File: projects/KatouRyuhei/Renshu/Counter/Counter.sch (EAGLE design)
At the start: 63 parts

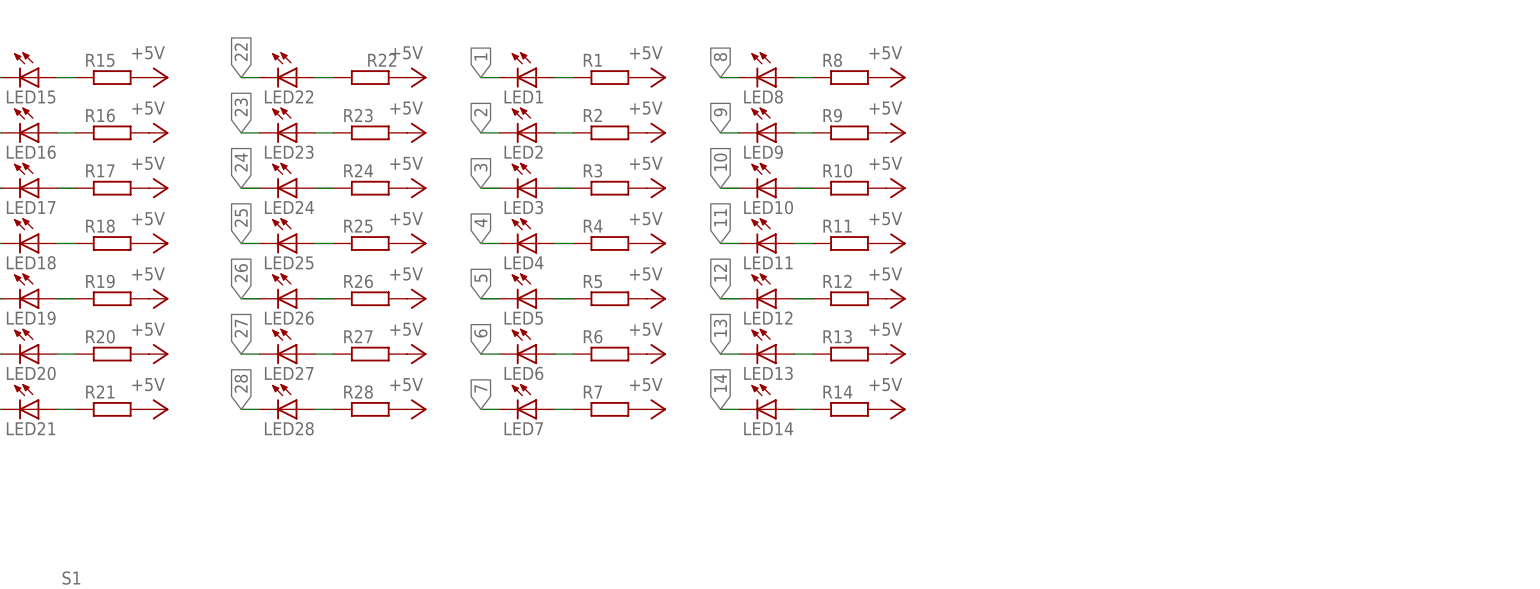
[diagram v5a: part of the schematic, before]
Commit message: 10進数2桁カウンタ製作途中
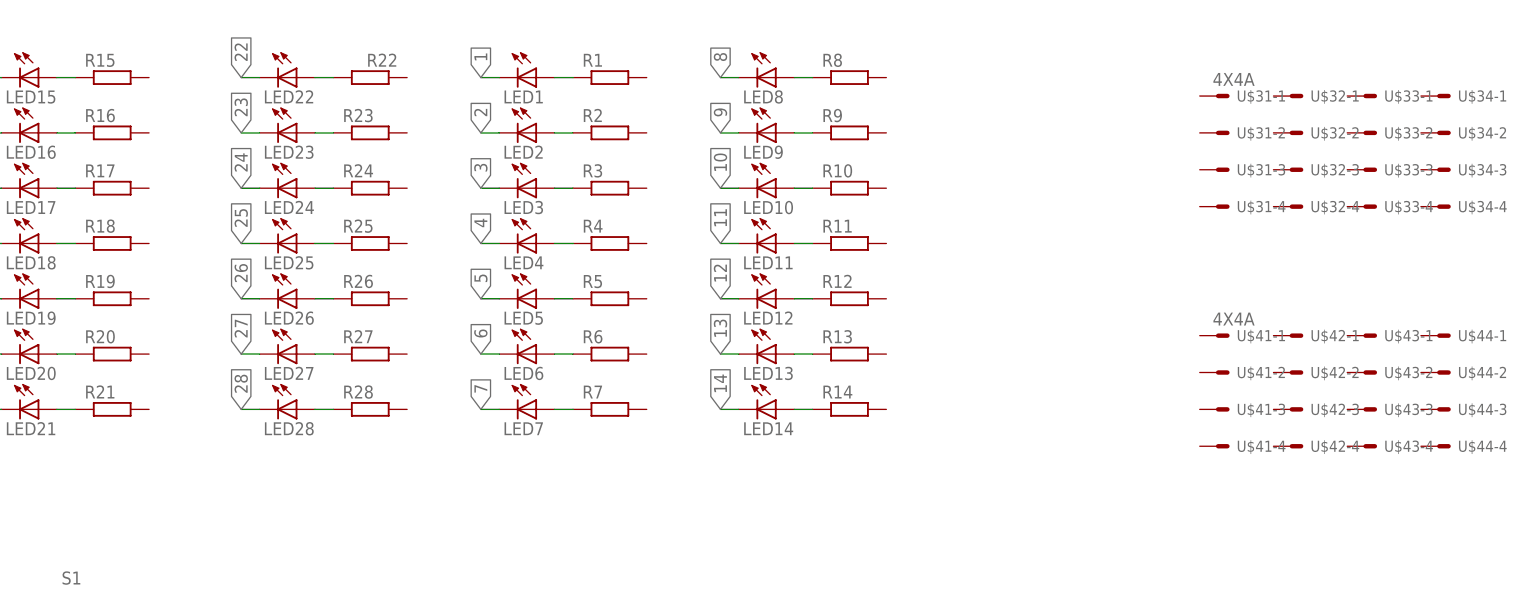
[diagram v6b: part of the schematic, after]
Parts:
- added U$3, U$4: 4X4A, 3M_372xx:4X4A
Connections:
- removed net +5V: R1.2, R10.2, R11.2, R12.2, R13.2, R14.2, R15.2, R16.2, R17.2, R18.2, R19.2, R2.2, R20.2, R21.2, R22.1, R23.2, R24.2, R25.2, R26.2, R27.2, R28.2, R3.2, R4.2, R5.2, R6.2, R7.2, R8.2, R9.2
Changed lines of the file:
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@@
 <part name="GND3" library="supply1" deviceset="GND" device=""/>
 <part name="GND4" library="supply1" deviceset="GND" device=""/>
-<part name="P+1" library="supply1" deviceset="+5V" device=""/>
-<part name="P+2" library="supply1" deviceset="+5V" device=""/>
-<part name="P+3" library="supply1" deviceset="+5V" device=""/>
-<part name="P+4" library="supply1" deviceset="+5V" device=""/>
-<part name="P+5" library="supply1" deviceset="+5V" device=""/>
-<part name="P+6" library="supply1" deviceset="+5V" device=""/>
-<part name="P+7" library="supply1" deviceset="+5V" device=""/>
-<part name="P+8" library="supply1" deviceset="+5V" device=""/>
-<part name="P+9" library="supply1" deviceset="+5V" device=""/>
-<part name="P+10" library="supply1" deviceset="+5V" device=""/>
-<part name="P+11" library="supply1" deviceset="+5V" device=""/>
-<part name="P+12" library="supply1" deviceset="+5V" device=""/>
-<part name="P+13" library="supply1" deviceset="+5V" device=""/>
-<part name="P+14" library="supply1" deviceset="+5V" device=""/>
-<part name="P+15" library="supply1" deviceset="+5V" device=""/>
-<part name="P+16" library="supply1" deviceset="+5V" device=""/>
-<part name="P+17" library="supply1" deviceset="+5V" device=""/>
-<part name="P+18" library="supply1" deviceset="+5V" device=""/>
-<part name="P+19" library="supply1" deviceset="+5V" device=""/>
-<part name="P+20" library="supply1" deviceset="+5V" device=""/>
-<part name="P+21" library="supply1" deviceset="+5V" device=""/>
-<part name="P+22" library="supply1" deviceset="+5V" device=""/>
-<part name="P+23" library="supply1" deviceset="+5V" device=""/>
-<part name="P+24" library="supply1" deviceset="+5V" device=""/>
-<part name="P+25" library="supply1" deviceset="+5V" device=""/>
-<part name="P+26" library="supply1" deviceset="+5V" device=""/>
-<part name="P+27" library="supply1" deviceset="+5V" device=""/>
-<part name="P+28" library="supply1" deviceset="+5V" device=""/>
+<part name="U$3" library="3M_372xx" deviceset="4X4" device="A"/>
+<part name="U$4" library="3M_372xx" deviceset="4X4" device="A"/>
 </parts>
 <sheets>
@@
 <instance part="GND3" gate="1" x="-218.44" y="17.78" rot="R270"/>
 <instance part="GND4" gate="1" x="-215.9" y="10.16"/>
-<instance part="P+1" gate="1" x="-109.22" y="81.28" rot="R270"/>
-<instance part="P+2" gate="1" x="-109.22" y="88.9" rot="R270"/>
-<instance part="P+3" gate="1" x="-109.22" y="96.52" rot="R270"/>
-<instance part="P+4" gate="1" x="-109.22" y="104.14" rot="R270"/>
-<instance part="P+5" gate="1" x="-109.22" y="111.76" rot="R270"/>
-<instance part="P+6" gate="1" x="-109.22" y="119.38" rot="R270"/>
-<instance part="P+7" gate="1" x="-109.22" y="127" rot="R270"/>
-<instance part="P+8" gate="1" x="-73.66" y="127" rot="R270"/>
-<instance part="P+9" gate="1" x="-73.66" y="119.38" rot="R270"/>
-<instance part="P+10" gate="1" x="-73.66" y="111.76" rot="R270"/>
-<instance part="P+11" gate="1" x="-73.66" y="104.14" rot="R270"/>
-<instance part="P+12" gate="1" x="-73.66" y="96.52" rot="R270"/>
-<instance part="P+13" gate="1" x="-73.66" y="88.9" rot="R270"/>
-<instance part="P+14" gate="1" x="-73.66" y="81.28" rot="R270"/>
-<instance part="P+15" gate="1" x="-40.64" y="81.28" rot="R270"/>
-<instance part="P+16" gate="1" x="-40.64" y="88.9" rot="R270"/>
-<instance part="P+17" gate="1" x="-40.64" y="96.52" rot="R270"/>
-<instance part="P+18" gate="1" x="-40.64" y="104.14" rot="R270"/>
-<instance part="P+19" gate="1" x="-40.64" y="111.76" rot="R270"/>
-<instance part="P+20" gate="1" x="-40.64" y="119.38" rot="R270"/>
-<instance part="P+21" gate="1" x="-40.64" y="127" rot="R270"/>
-<instance part="P+22" gate="1" x="-7.62" y="127" rot="R270"/>
-<instance part="P+23" gate="1" x="-7.62" y="119.38" rot="R270"/>
-<instance part="P+24" gate="1" x="-7.62" y="111.76" rot="R270"/>
-<instance part="P+25" gate="1" x="-7.62" y="104.14" rot="R270"/>
-<instance part="P+26" gate="1" x="-7.62" y="96.52" rot="R270"/>
-<instance part="P+27" gate="1" x="-7.62" y="88.9" rot="R270"/>
-<instance part="P+28" gate="1" x="-7.62" y="81.28" rot="R270"/>
+<instance part="U$3" gate="2-1" x="48.26" y="124.46"/>
+<instance part="U$3" gate="2-2" x="48.26" y="119.38"/>
+<instance part="U$3" gate="2-3" x="48.26" y="114.3"/>
+<instance part="U$3" gate="2-4" x="48.26" y="109.22"/>
+<instance part="U$3" gate="3-1" x="58.42" y="124.46"/>
+<instance part="U$3" gate="3-2" x="58.42" y="119.38"/>
+<instance part="U$3" gate="3-3" x="58.42" y="114.3"/>
+<instance part="U$3" gate="3-4" x="58.42" y="109.22"/>
+<instance part="U$3" gate="1-2" x="38.1" y="119.38"/>
+<instance part="U$3" gate="1-3" x="38.1" y="114.3"/>
+<instance part="U$3" gate="1-4" x="38.1" y="109.22"/>
+<instance part="U$3" gate="4-1" x="68.58" y="124.46"/>
+<instance part="U$3" gate="4-2" x="68.58" y="119.38"/>
+<instance part="U$3" gate="4-3" x="68.58" y="114.3"/>
+<instance part="U$3" gate="4-4" x="68.58" y="109.22"/>
+<instance part="U$3" gate="1-1" x="38.1" y="124.46"/>
+<instance part="U$4" gate="2-1" x="48.26" y="91.44"/>
+<instance part="U$4" gate="2-2" x="48.26" y="86.36"/>
+<instance part="U$4" gate="2-3" x="48.26" y="81.28"/>
+<instance part="U$4" gate="2-4" x="48.26" y="76.2"/>
+<instance part="U$4" gate="3-1" x="58.42" y="91.44"/>
+<instance part="U$4" gate="3-2" x="58.42" y="86.36"/>
+<instance part="U$4" gate="3-3" x="58.42" y="81.28"/>
+<instance part="U$4" gate="3-4" x="58.42" y="76.2"/>
+<instance part="U$4" gate="1-2" x="38.1" y="86.36"/>
+<instance part="U$4" gate="1-3" x="38.1" y="81.28"/>
+<instance part="U$4" gate="1-4" x="38.1" y="76.2"/>
+<instance part="U$4" gate="4-1" x="68.58" y="91.44"/>
+<instance part="U$4" gate="4-2" x="68.58" y="86.36"/>
+<instance part="U$4" gate="4-3" x="68.58" y="81.28"/>
+<instance part="U$4" gate="4-4" x="68.58" y="76.2"/>
+<instance part="U$4" gate="1-1" x="38.1" y="91.44"/>
 </instances>
 <busses>
@@
 </segment>
 </net>
-<net name="+5V" class="0">
-<segment>
-<pinref part="R21" gate="G$1" pin="2"/>
-<pinref part="P+1" gate="1" pin="+5V"/>
-</segment>
-<segment>
-<pinref part="R20" gate="G$1" pin="2"/>
-<pinref part="P+2" gate="1" pin="+5V"/>
-</segment>
-<segment>
-<pinref part="R19" gate="G$1" pin="2"/>
-<pinref part="P+3" gate="1" pin="+5V"/>
-</segment>
-<segment>
-<pinref part="R18" gate="G$1" pin="2"/>
-<pinref part="P+4" gate="1" pin="+5V"/>
-</segment>
-<segment>
-<pinref part="R17" gate="G$1" pin="2"/>
-<pinref part="P+5" gate="1" pin="+5V"/>
-</segment>
-<segment>
-<pinref part="R16" gate="G$1" pin="2"/>
-<pinref part="P+6" gate="1" pin="+5V"/>
-</segment>
-<segment>
-<pinref part="R15" gate="G$1" pin="2"/>
-<pinref part="P+7" gate="1" pin="+5V"/>
-</segment>
-<segment>
-<pinref part="R22" gate="G$1" pin="1"/>
-<pinref part="P+8" gate="1" pin="+5V"/>
-</segment>
-<segment>
-<pinref part="R23" gate="G$1" pin="2"/>
-<pinref part="P+9" gate="1" pin="+5V"/>
-</segment>
-<segment>
-<pinref part="R24" gate="G$1" pin="2"/>
-<pinref part="P+10" gate="1" pin="+5V"/>
-</segment>
-<segment>
-<pinref part="R25" gate="G$1" pin="2"/>
-<pinref part="P+11" gate="1" pin="+5V"/>
-</segment>
-<segment>
-<pinref part="R26" gate="G$1" pin="2"/>
-<pinref part="P+12" gate="1" pin="+5V"/>
-</segment>
-<segment>
-<pinref part="R27" gate="G$1" pin="2"/>
-<pinref part="P+13" gate="1" pin="+5V"/>
-</segment>
-<segment>
-<pinref part="R28" gate="G$1" pin="2"/>
-<pinref part="P+14" gate="1" pin="+5V"/>
-</segment>
-<segment>
-<pinref part="R7" gate="G$1" pin="2"/>
-<pinref part="P+15" gate="1" pin="+5V"/>
-</segment>
-<segment>
-<pinref part="R6" gate="G$1" pin="2"/>
-<pinref part="P+16" gate="1" pin="+5V"/>
-</segment>
-<segment>
-<pinref part="R5" gate="G$1" pin="2"/>
-<pinref part="P+17" gate="1" pin="+5V"/>
-</segment>
-<segment>
-<pinref part="R4" gate="G$1" pin="2"/>
-<pinref part="P+18" gate="1" pin="+5V"/>
-</segment>
-<segment>
-<pinref part="R3" gate="G$1" pin="2"/>
-<pinref part="P+19" gate="1" pin="+5V"/>
-</segment>
-<segment>
-<pinref part="R2" gate="G$1" pin="2"/>
-<pinref part="P+20" gate="1" pin="+5V"/>
-</segment>
-<segment>
-<pinref part="R1" gate="G$1" pin="2"/>
-<pinref part="P+21" gate="1" pin="+5V"/>
-</segment>
-<segment>
-<pinref part="R8" gate="G$1" pin="2"/>
-<pinref part="P+22" gate="1" pin="+5V"/>
-</segment>
-<segment>
-<pinref part="R9" gate="G$1" pin="2"/>
-<pinref part="P+23" gate="1" pin="+5V"/>
-</segment>
-<segment>
-<pinref part="R10" gate="G$1" pin="2"/>
-<pinref part="P+24" gate="1" pin="+5V"/>
-</segment>
-<segment>
-<pinref part="R11" gate="G$1" pin="2"/>
-<pinref part="P+25" gate="1" pin="+5V"/>
-</segment>
-<segment>
-<pinref part="R12" gate="G$1" pin="2"/>
-<pinref part="P+26" gate="1" pin="+5V"/>
-</segment>
-<segment>
-<pinref part="R13" gate="G$1" pin="2"/>
-<pinref part="P+27" gate="1" pin="+5V"/>
-</segment>
-<segment>
-<pinref part="R14" gate="G$1" pin="2"/>
-<pinref part="P+28" gate="1" pin="+5V"/>
-</segment>
-</net>

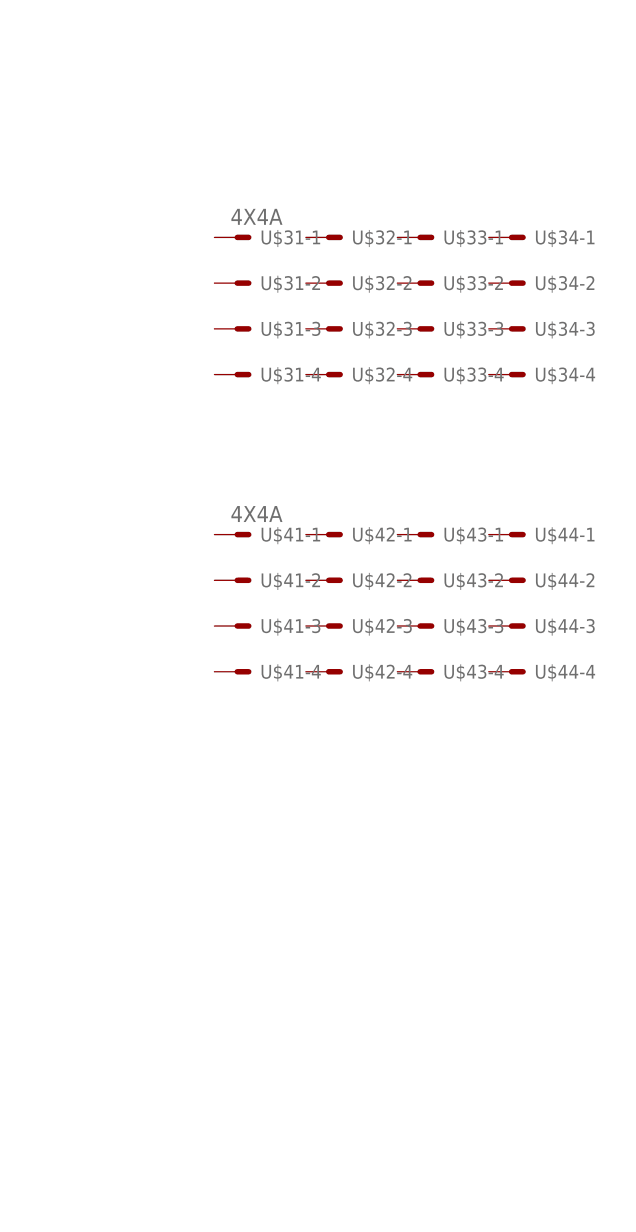
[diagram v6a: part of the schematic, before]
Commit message: 10進数2桁カウンタ製作途中
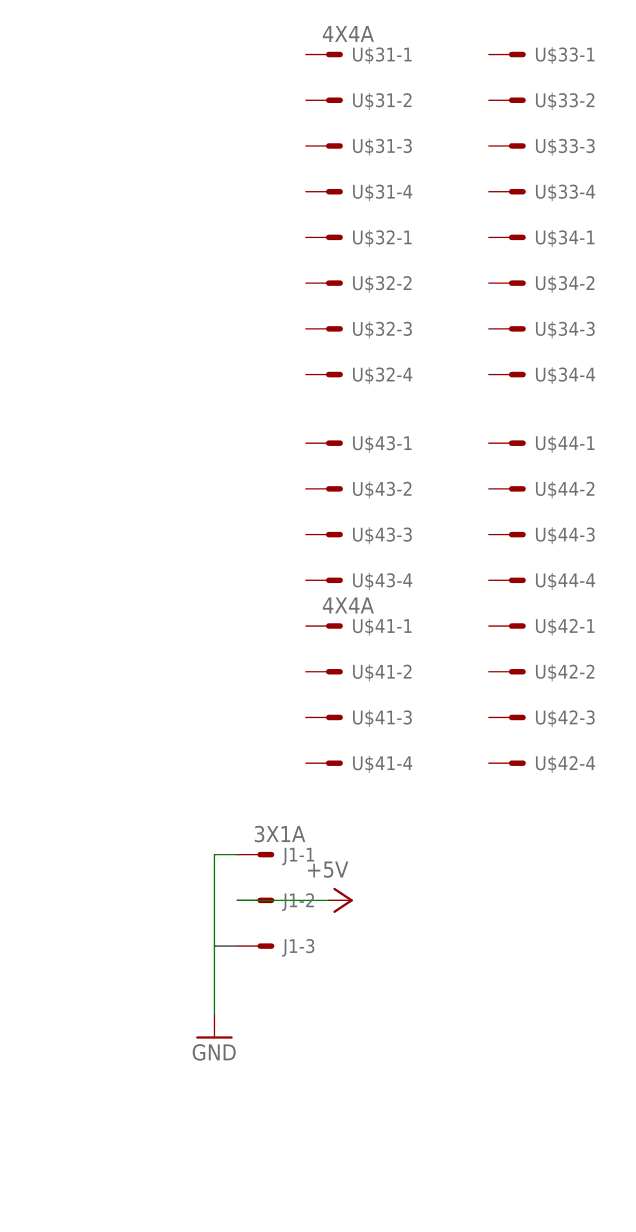
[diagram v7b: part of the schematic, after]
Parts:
- added J1: 3X1A, 3M_372xx:3X1A
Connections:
- new net +5V: J1-2.S
- net GND: now also J1-1.S, J1-3.S
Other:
- moved on the sheet: U$31-1, U$31-2, U$31-3, U$31-4, U$33-1, U$33-2, U$33-3, U$33-4, U$41-1, U$41-2, U$41-3, U$41-4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
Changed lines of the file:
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@@
 <part name="U$3" library="3M_372xx" deviceset="4X4" device="A"/>
 <part name="U$4" library="3M_372xx" deviceset="4X4" device="A"/>
+<part name="J1" library="3M_372xx" deviceset="3X1" device="A"/>
+<part name="GND5" library="supply1" deviceset="GND" device=""/>
+<part name="P+1" library="supply1" deviceset="+5V" device=""/>
 </parts>
 <sheets>
@@
 <instance part="U$3" gate="2-3" x="48.26" y="114.3"/>
 <instance part="U$3" gate="2-4" x="48.26" y="109.22"/>
-<instance part="U$3" gate="3-1" x="58.42" y="124.46"/>
-<instance part="U$3" gate="3-2" x="58.42" y="119.38"/>
-<instance part="U$3" gate="3-3" x="58.42" y="114.3"/>
-<instance part="U$3" gate="3-4" x="58.42" y="109.22"/>
-<instance part="U$3" gate="1-2" x="38.1" y="119.38"/>
-<instance part="U$3" gate="1-3" x="38.1" y="114.3"/>
-<instance part="U$3" gate="1-4" x="38.1" y="109.22"/>
+<instance part="U$3" gate="3-1" x="68.58" y="144.78"/>
+<instance part="U$3" gate="3-2" x="68.58" y="139.7"/>
+<instance part="U$3" gate="3-3" x="68.58" y="134.62"/>
+<instance part="U$3" gate="3-4" x="68.58" y="129.54"/>
+<instance part="U$3" gate="1-2" x="48.26" y="139.7"/>
+<instance part="U$3" gate="1-3" x="48.26" y="134.62"/>
+<instance part="U$3" gate="1-4" x="48.26" y="129.54"/>
 <instance part="U$3" gate="4-1" x="68.58" y="124.46"/>
 <instance part="U$3" gate="4-2" x="68.58" y="119.38"/>
 <instance part="U$3" gate="4-3" x="68.58" y="114.3"/>
 <instance part="U$3" gate="4-4" x="68.58" y="109.22"/>
-<instance part="U$3" gate="1-1" x="38.1" y="124.46"/>
-<instance part="U$4" gate="2-1" x="48.26" y="91.44"/>
-<instance part="U$4" gate="2-2" x="48.26" y="86.36"/>
-<instance part="U$4" gate="2-3" x="48.26" y="81.28"/>
-<instance part="U$4" gate="2-4" x="48.26" y="76.2"/>
-<instance part="U$4" gate="3-1" x="58.42" y="91.44"/>
-<instance part="U$4" gate="3-2" x="58.42" y="86.36"/>
-<instance part="U$4" gate="3-3" x="58.42" y="81.28"/>
-<instance part="U$4" gate="3-4" x="58.42" y="76.2"/>
-<instance part="U$4" gate="1-2" x="38.1" y="86.36"/>
-<instance part="U$4" gate="1-3" x="38.1" y="81.28"/>
-<instance part="U$4" gate="1-4" x="38.1" y="76.2"/>
-<instance part="U$4" gate="4-1" x="68.58" y="91.44"/>
-<instance part="U$4" gate="4-2" x="68.58" y="86.36"/>
-<instance part="U$4" gate="4-3" x="68.58" y="81.28"/>
-<instance part="U$4" gate="4-4" x="68.58" y="76.2"/>
-<instance part="U$4" gate="1-1" x="38.1" y="91.44"/>
+<instance part="U$3" gate="1-1" x="48.26" y="144.78"/>
+<instance part="U$4" gate="2-1" x="68.58" y="81.28"/>
+<instance part="U$4" gate="2-2" x="68.58" y="76.2"/>
+<instance part="U$4" gate="2-3" x="68.58" y="71.12"/>
+<instance part="U$4" gate="2-4" x="68.58" y="66.04"/>
+<instance part="U$4" gate="3-1" x="48.26" y="101.6"/>
+<instance part="U$4" gate="3-2" x="48.26" y="96.52"/>
+<instance part="U$4" gate="3-3" x="48.26" y="91.44"/>
+<instance part="U$4" gate="3-4" x="48.26" y="86.36"/>
+<instance part="U$4" gate="1-2" x="48.26" y="76.2"/>
+<instance part="U$4" gate="1-3" x="48.26" y="71.12"/>
+<instance part="U$4" gate="1-4" x="48.26" y="66.04"/>
+<instance part="U$4" gate="4-1" x="68.58" y="101.6"/>
+<instance part="U$4" gate="4-2" x="68.58" y="96.52"/>
+<instance part="U$4" gate="4-3" x="68.58" y="91.44"/>
+<instance part="U$4" gate="4-4" x="68.58" y="86.36"/>
+<instance part="U$4" gate="1-1" x="48.26" y="81.28"/>
+<instance part="J1" gate="-1" x="40.64" y="55.88"/>
+<instance part="J1" gate="-2" x="40.64" y="50.8"/>
+<instance part="J1" gate="-3" x="40.64" y="45.72"/>
+<instance part="GND5" gate="1" x="33.02" y="35.56"/>
+<instance part="P+1" gate="1" x="48.26" y="50.8" rot="R270"/>
 </instances>
 <busses>
@@
 <wire x1="-215.9" y1="15.24" x2="-215.9" y2="12.7" width="0.1524" layer="91"/>
 </segment>
+<segment>
+<pinref part="J1" gate="-1" pin="S"/>
+<wire x1="35.56" y1="55.88" x2="33.02" y2="55.88" width="0.1524" layer="91"/>
+<wire x1="33.02" y1="55.88" x2="33.02" y2="45.72" width="0.1524" layer="91"/>
+<pinref part="J1" gate="-3" pin="S"/>
+<wire x1="33.02" y1="45.72" x2="33.02" y2="38.1" width="0.1524" layer="91"/>
+<wire x1="35.56" y1="45.72" x2="33.02" y2="45.72" width="0.1524" layer="91"/>
+<pinref part="GND5" gate="1" pin="GND"/>
+</segment>
 </net>
 <net name="1" class="0">
@@
 </segment>
 </net>
+<net name="+5V" class="0">
+<segment>
+<pinref part="J1" gate="-2" pin="S"/>
+<wire x1="35.56" y1="50.8" x2="45.72" y2="50.8" width="0.1524" layer="91"/>
+<pinref part="P+1" gate="1" pin="+5V"/>
+</segment>
+</net>
